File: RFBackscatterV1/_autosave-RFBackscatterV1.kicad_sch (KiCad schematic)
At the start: 9 parts, among them J1 SMA-J-P-H-RA-TH1, U1 SIT1534AI-H4-DCC-00.001E

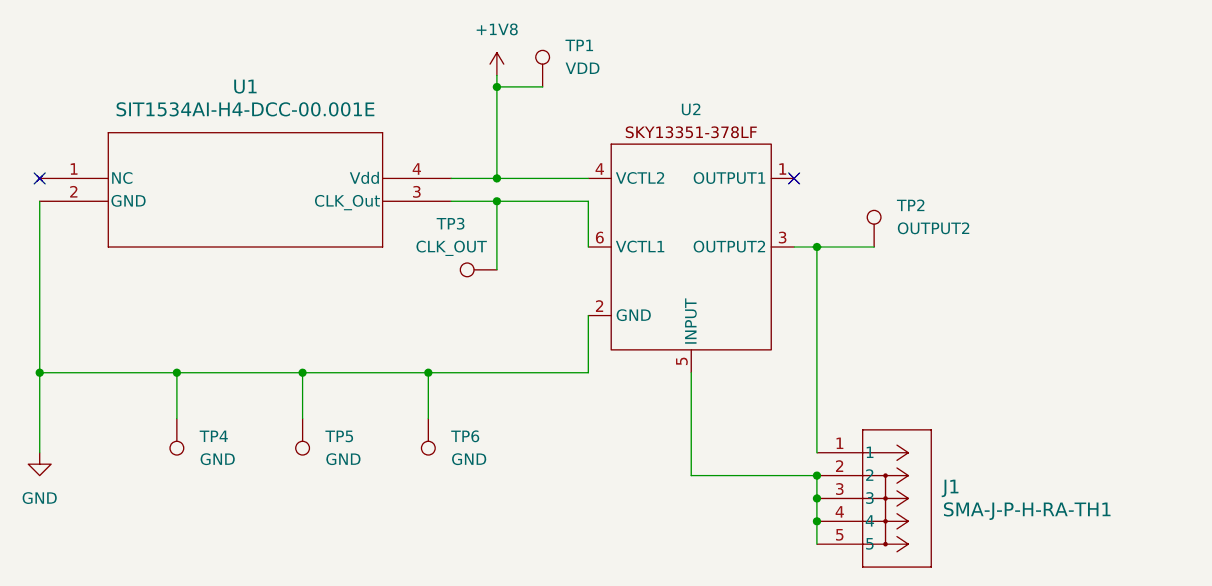
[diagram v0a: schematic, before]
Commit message: updated board, added buffer and filter capacitors
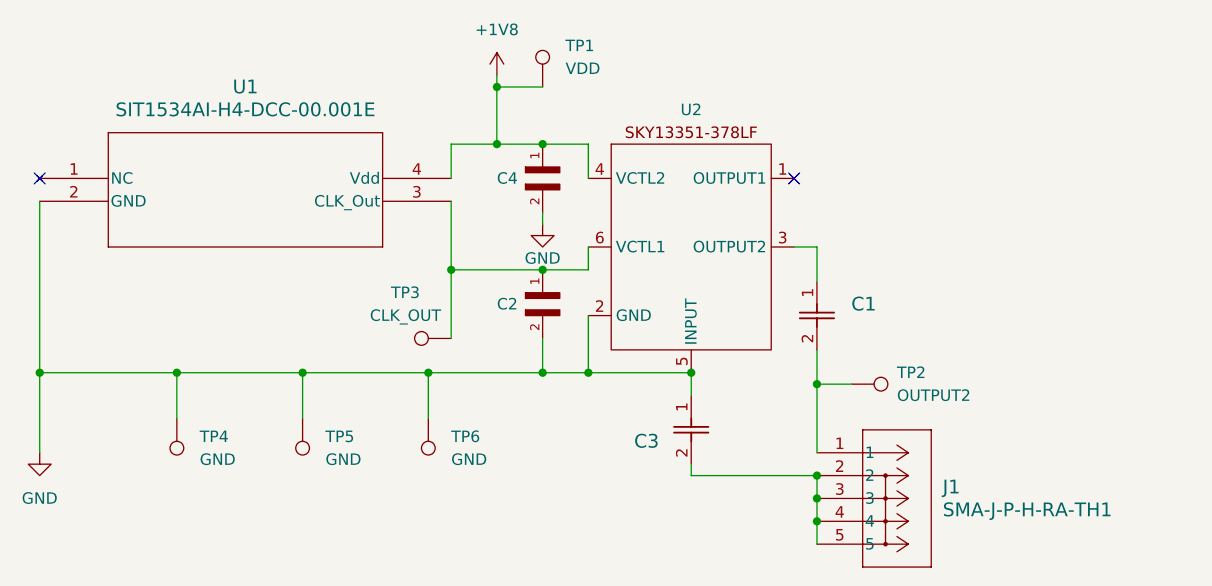
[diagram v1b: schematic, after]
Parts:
- added C1: CBR04C101J3GAC, WADARfootprints:CAPC10555_55N_KEM, symbol CBR04C101J3GAC:CBR04C101J3GAC
- added C2, C4: GJM1555C1H330JB01D, WADARfootprints:CAPC10555_55N_KEM, symbol GJM1555C1H330JB01D:GJM1555C1H330JB01D
- added C3: CBR04C101J3GAC, CAPC10555_55N_KEM, symbol CBR04C101J3GAC:CBR04C101J3GAC
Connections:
- net +1V8: now also C4.1
- net GND: now also U2.5 (INPUT), C2.2, C3.1, C4.2
- net at J1.1, TP2.1: now also C1.2; no longer U2.3 (OUTPUT2)
- net at J1.2, J1.3, J1.4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: now also C3.2; no longer U2.5 (INPUT)
- net at TP3.1, U1.3 (CLK_Out), U2.6 (VCTL1): now also C2.1
- new net: C1.1, U2.3 (OUTPUT2)
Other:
- moved on the sheet: TP2, TP3
